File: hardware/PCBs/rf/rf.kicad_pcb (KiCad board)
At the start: 4 copper layers, 54 parts, among them IC8 SI4468-A2A-IMR, J1 PH1-08-UA, J5 RFPC-SMA28-F, Q6 DMN1008UFDF-7

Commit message: RF finished
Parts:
- moved C17 25.8 mm to (163.5, 70.5)
- moved C18 25.8 mm to (161.5, 73.2)
- moved C19 25.8 mm to (155.2, 76.0)
- moved C20 25.8 mm to (157.0, 73.5)
- moved C21 25.8 mm to (136.2, 78.0)
- moved C22 25.8 mm to (133.0, 78.0)
- moved C23 25.8 mm to (160.5, 80.2)
- moved C24 25.8 mm to (158.2, 86.0)
- moved C25 25.8 mm to (158.3, 83.8)
- moved C26 25.8 mm to (158.5, 81.2)
- moved C27 25.8 mm to (159.0, 79.8)
- moved C28 25.8 mm to (155.2, 79.5)
- moved C29 25.8 mm to (154.7, 77.5)
- moved C30 25.8 mm to (150.8, 77.5)
- moved C31 25.8 mm to (146.2, 77.9)
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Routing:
- net Net-(C32-Pad1): track 1.22 -> 4.11 mm
- net GND: track 4.64 -> 7.05 mm, vias 6 -> 147
- net +3V3: track 14.3 -> 16.6 mm, vias 4 -> 8
- net (no net): vias 4 -> 0
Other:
- board outline added: 96 x 90 mm
- board text added: "Jan Kusak"

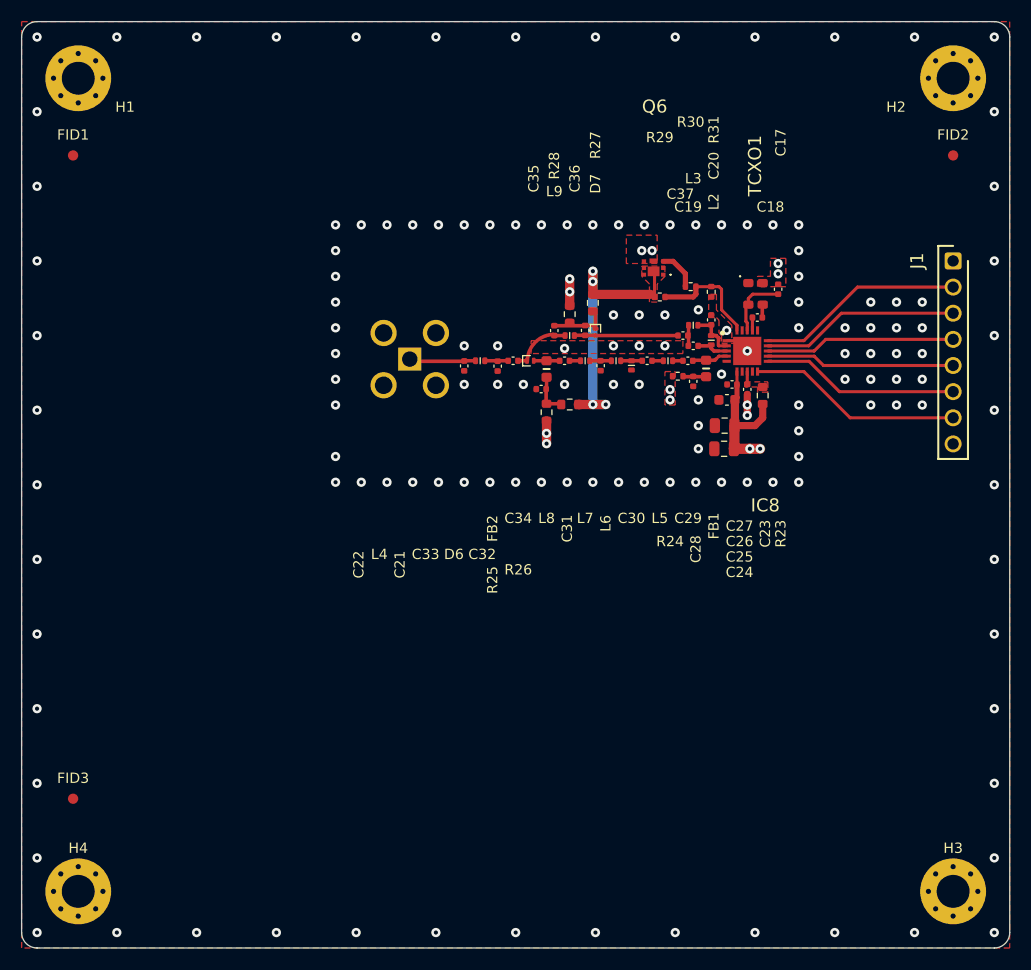
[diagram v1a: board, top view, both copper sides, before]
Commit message: PCB - RF done, 1/2 MCU
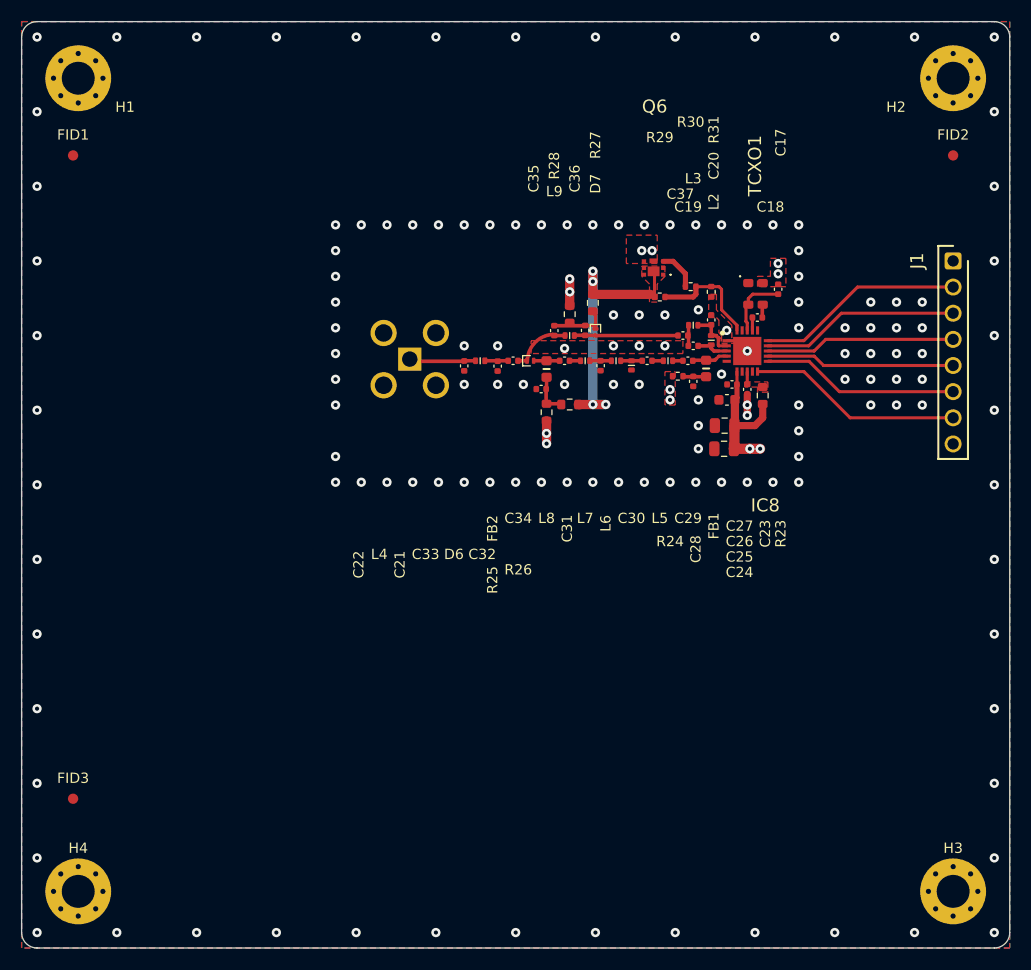
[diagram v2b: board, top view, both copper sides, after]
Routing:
- added copper zone on B.Cu, net GND
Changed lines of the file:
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@@
 		(tags "Diode")
 		(property "Reference" "D7"
-			(at 0 14.425 270)
+			(at 0 14.425 -90)
 			(layer "F.SilkS")
 			(effects
@@
 		(layer "F.Cu")
 		(hatch edge 0.5)
-		(connect_pads yes
-			(clearance 0.6)
-		)
-		(min_thickness 0.25)
-		(filled_areas_thickness no)
-		(fill yes
-			(thermal_gap 0.4)
-			(thermal_bridge_width 0.25)
-		)
-		(polygon
-			(pts
-				(xy 90 44.5) (xy 186 44.5) (xy 186 134.5) (xy 90 134.5)
-			)
-		)
-	)
-	(zone
-		(net 8)
-		(net_name "GND")
-		(layer "F.Cu")
-		(hatch edge 0.5)
 		(priority 7)
 		(connect_pads yes
@@
 			)
 		)
+	)
+	(zone
+		(net 8)
+		(net_name "GND")
+		(layers "F&B.Cu")
+		(hatch edge 0.5)
+		(connect_pads yes
+			(clearance 0.6)
+		)
+		(min_thickness 0.25)
+		(filled_areas_thickness no)
+		(fill yes
+			(thermal_gap 0.4)
+			(thermal_bridge_width 0.25)
+		)
+		(polygon
+			(pts
+				(xy 90 44.5) (xy 186 44.5) (xy 186 134.5) (xy 90 134.5)
+			)
+		)

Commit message: Done? Rev.:1.2
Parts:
- moved C32 2.80 mm to (140.5, 83.0)
- moved C17 2.75 mm to (163.5, 73.2)
- moved C18 2.75 mm to (161.5, 76.0)
- moved C19 2.75 mm to (155.2, 78.8)
- moved C20 2.75 mm to (157.0, 76.2)
- moved C21 2.75 mm to (136.2, 80.7)
- moved C22 2.75 mm to (133.0, 80.7)
- moved C23 2.75 mm to (160.5, 83.0)
- moved C24 2.75 mm to (158.2, 88.8)
- moved C25 2.75 mm to (158.3, 86.5)
- moved C26 2.75 mm to (158.5, 84.0)
- moved C27 2.75 mm to (159.0, 82.5)
- moved C28 2.75 mm to (155.2, 82.2)
- moved C29 2.75 mm to (154.7, 80.2)
- moved C30 2.75 mm to (150.8, 80.2)
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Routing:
- net GND: track 7.05 -> 2.79 mm, vias 147 -> 161
- net /SW: track 27.7 -> 28.6 mm

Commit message: gitignore added
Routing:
- net GND: vias 161 -> 164
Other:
- board text added: "3V3"
- board text added: "DONE"
- board text added: "GND"
- board text added: "SCLK"
- board text added: "SDI"
- board text added: "SDO"
- board text added: "nIRQ"
- board text added: "nSEL"
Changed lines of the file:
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@@
 		(solder_mask_min_width 0.125)
 		(allow_soldermask_bridges_in_footprints no)
+		(aux_axis_origin 90 134.5)
+		(grid_origin 90 134.5)
 		(pcbplotparams
-			(layerselection 0x00010fc_ffffffff)
+			(layerselection 0x00010f8_ffffffff)
 			(plot_on_all_layers_selection 0x0000000_00000000)
 			(disableapertmacros no)
@@
 			(viasonmask no)
 			(mode 1)
-			(useauxorigin no)
+			(useauxorigin yes)
 			(hpglpennumber 1)
 			(hpglpenspeed 20)
@@
 			(psnegative no)
 			(psa4output no)
-			(plotreference yes)
-			(plotvalue yes)
-			(plotfptext yes)
+			(plotreference no)
+			(plotvalue no)
+			(plotfptext no)
 			(plotinvisibletext no)
 			(sketchpadsonfab no)
@@
 			(outputformat 1)
 			(mirror no)
-			(drillshape 1)
+			(drillshape 0)
 			(scaleselection 1)
-			(outputdirectory "")
+			(outputdirectory "gerber/")
 		)
 	)
@@
 		(tags "Connector")
 		(property "Reference" "J1"
-			(at 0 3.5 90)
+			(at -3.5 0 90)
 			(layer "F.SilkS")
 			(effects
@@
 			(pintype "passive")
 		)
-		(model "C:\\Users\\honzu\\OneDrive\\Dokumenty\\KiCad\\SamacSys_Parts.3dshapes\\SI4468-A2A-IMR.stp"
+		(model "${KIPRJMOD}/3rdparty/SamacSys_Parts.3dshapes/SI4468-A2A-IMR.stp"
 			(offset
 				(xyz 0 0 0)
@@
 		(layer "Edge.Cuts")
 	)
+	(gr_text "DONE"
+		(at 171.25 86.75 0)
+		(layer "B.SilkS")
+		(effects
+			(font
+				(size 1 1)
+				(thickness 0.15)
+			)
+			(justify left bottom mirror)
+		)
+	)
+	(gr_text "GND"
+		(at 171.5 89.25 0)
+		(layer "B.SilkS")
+		(effects
+			(font
+				(size 1 1)
+				(thickness 0.15)
+			)
+			(justify left bottom mirror)
+		)
+	)
+	(gr_text "nSEL"
+		(at 171 74 0)
+		(layer "B.SilkS")
+		(effects
+			(font
+				(size 1 1)
+				(thickness 0.15)
+			)
+			(justify left bottom mirror)
+		)
+	)
+	(gr_text "SCLK"
+		(at 169.5 81.75 0)
+		(layer "B.SilkS")
+		(effects
+			(font
+				(size 1 1)
+				(thickness 0.15)
+			)
+			(justify left bottom mirror)
+		)
+	)
+	(gr_text "SDI"
+		(at 169.5 76.75 0)
+		(layer "B.SilkS")
+		(effects
+			(font
+				(size 1 1)
+				(thickness 0.15)
+			)
+			(justify left bottom mirror)
+		)
+	)
+	(gr_text "3V3"
+		(at 171 71.5 0)
+		(layer "B.SilkS")
+		(effects
+			(font
+				(size 1 1)
+				(thickness 0.15)
+			)
+			(justify left bottom mirror)
+		)
+	)
+	(gr_text "nIRQ"
+		(at 171.25 84.25 0)
+		(layer "B.SilkS")
+		(effects
+			(font
+				(size 1 1)
+				(thickness 0.15)
+			)
+			(justify left bottom mirror)
+		)
+	)
+	(gr_text "SDO"
+		(at 169.5 79.25 0)
+		(layer "B.SilkS")
+		(effects
+			(font
+				(size 1 1)
+				(thickness 0.15)
+			)
+			(justify left bottom mirror)
+		)
+	)
 	(gr_text "Jan Kusak"
 		(at 125.25 124.75 0)
@@
 	)
 	(via
+		(at 157 75.5)
+		(size 0.9)
+		(drill 0.4)
+		(layers "F.Cu" "B.Cu")
+		(net 8)
+	)
+	(via
 		(at 150 78.75)
 		(size 0.9)
@@
 	)
 	(via
+		(at 120.5 87)
+		(size 0.9)
+		(drill 0.4)
+		(layers "F.Cu" "B.Cu")
+		(free yes)
+		(net 8)
+	)
+	(via
 		(at 91.5 118.5)
 		(size 0.9)
@@
 	)
 	(via
-		(at 143.25 73.5)
+		(at 143.25 73.75)
 		(size 0.9)
 		(drill 0.4)
@@
 	)
 	(via
-		(at 155.75 75.25)
+		(at 157 74.25)
 		(size 0.9)
 		(drill 0.4)
@@
 	)
 	(via
-		(at 142 74.75)
+		(at 143.25 74.75)
 		(size 0.9)
 		(drill 0.4)
@@
 	)
 	(via
+		(at 156 75)
+		(size 0.9)
+		(drill 0.4)
+		(layers "F.Cu" "B.Cu")
+		(free yes)
+		(net 8)
+	)
+	(via
 		(at 91.5 125.75)
 		(size 0.9)
@@
 	)
 	(segment
-		(start 132.93 80.29)
-		(end 133 80.22)
-		(width 0.3493)
-		(layer "F.Cu")
-		(net 10)
-	)
-	(segment
 		(start 160.5 81.25)
 		(end 160.5 82.5)
@@
 	)
 	(segment
-		(start 145.5 72.5)
-		(end 145.5 71.5)
-		(width 0.9)
+		(start 151.165 73.675)
+		(end 151.49 74)
+		(width 0.3)
 		(layer "F.Cu")
 		(net 36)
 	)
 	(segment
-		(start 151.165 73.675)
-		(end 151.49 74)
-		(width 0.3)
+		(start 145.5 72.5)
+		(end 145.5 71.5)
+		(width 0.9)
 		(layer "F.Cu")
 		(net 36)
@@
 	)
 	(segment
-		(start 144.5 72.5)
-		(end 144.5 83.5)
+		(start 144.5 83.5)
+		(end 145.45 84.45)
 		(width 0.9)
 		(layer "B.Cu")
@@
 	)
 	(segment
-		(start 145.5 71.5)
-		(end 144.5 72.5)
+		(start 144.5 73.5)
+		(end 144.5 83.5)
 		(width 0.9)
 		(layer "B.Cu")
@@
 	)
 	(segment
+		(start 145.5 72.5)
+		(end 144.5 73.5)
+		(width 0.9)
+		(layer "B.Cu")
+		(net 36)
+	)
+	(segment
 		(start 145.5 84.45)
 		(end 146.75 84.45)
@@
 	)
 	(segment
-		(start 144.5 83.5)
-		(end 145.45 84.45)
+		(start 145.5 72.5)
+		(end 145.5 71.5)
 		(width 0.9)
 		(layer "B.Cu")
